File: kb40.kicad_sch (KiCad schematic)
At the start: 79 parts, among them SW1 Choc, SW10 Choc, SW11 Choc, SW12 Choc, SW13 Choc, SW14 Choc, SW15 Choc, SW16 Choc, SW17 Choc, SW18 Choc, SW19 Choc, SW2 Choc, SW20 Choc, SW21 Choc, SW22 Choc, SW23 Choc, SW24 Choc, SW3 Choc, SW4 Choc, SW5 Choc, SW6 Choc, SW7 Choc, SW8 Choc, SW9 Choc, U1 ProMicro

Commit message: initial layout
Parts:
- removed LED25, LED26, LED27, LED28, LED29, LED30: SK6812MINI-E, LED_SMD:LED_SK6812MINI_PLCC4_3.5x3.5mm_P1.75mm, symbol LED:SK6812MINI
- D1, D10, D11, D12, D13, D14, D15, D16, D17, D18, D19, D2, D20, D21, D22, D23, D24, D3, D4, D5, D6, D7, D8, D9: footprint (none) -> reversible-kicad-footprints:D_SOD-123
- LED1, LED10, LED11, LED12, LED13, LED14, LED15, LED16, LED17, LED18, LED19, LED2, LED20, LED21, LED22, LED23, LED24, LED3, LED4, LED5, LED6, LED7, LED8, LED9: footprint LED_SMD:LED_SK6812MINI_PLCC4_3.5x3.5mm_P1.75mm -> tufourn-components:SK6812Mini-E
- SW1, SW10, SW11, SW12, SW13, SW14, SW15, SW16, SW17, SW18, SW19, SW2, SW20, SW21, SW22, SW23, SW24, SW3, SW4, SW5, SW6, SW7, SW8, SW9: footprint (none) -> tufourn-components:Kailh_socket_PG1350_reversible
- U1: footprint (none) -> pro-micro:ProMicro
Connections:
- net LED: now reaches LED1.3 (DIN)
- no-connect marks 0 -> 1

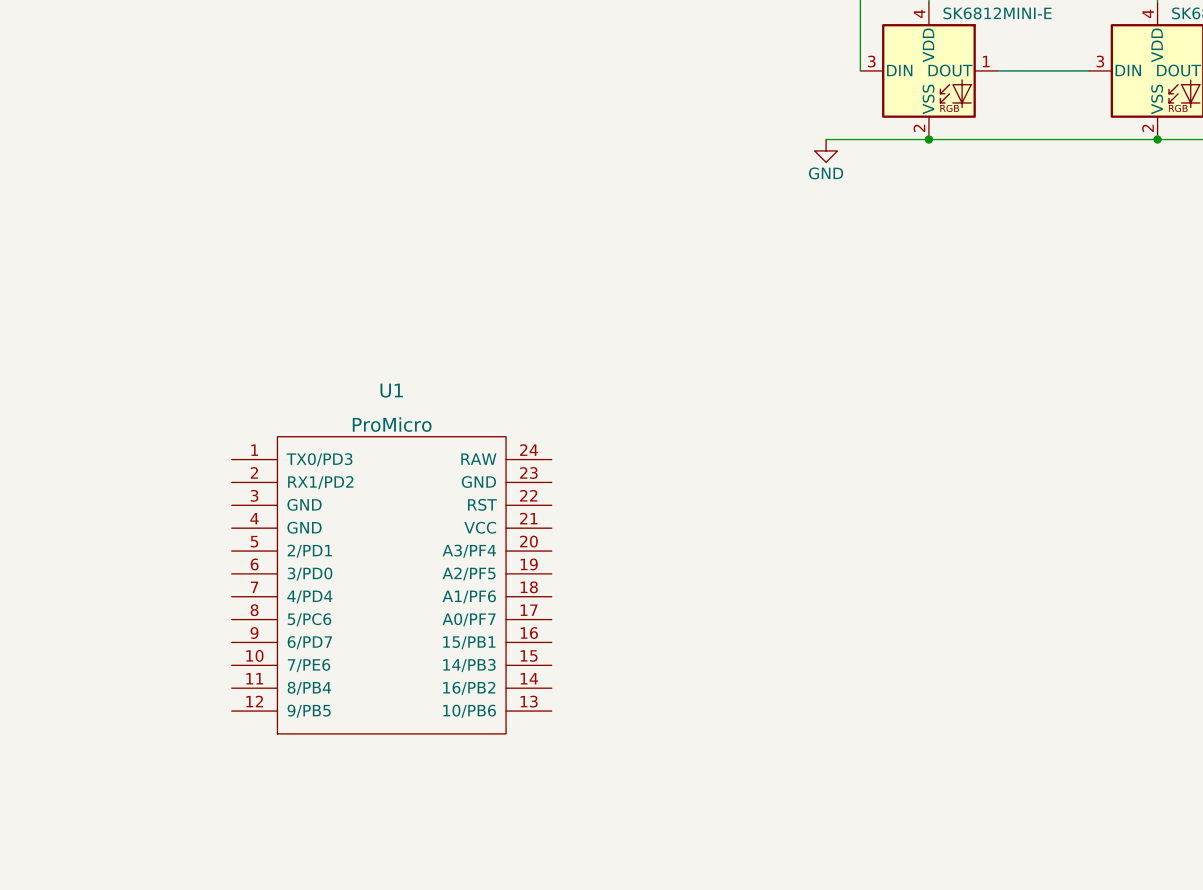
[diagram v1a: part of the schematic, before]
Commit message: initial matrix routing
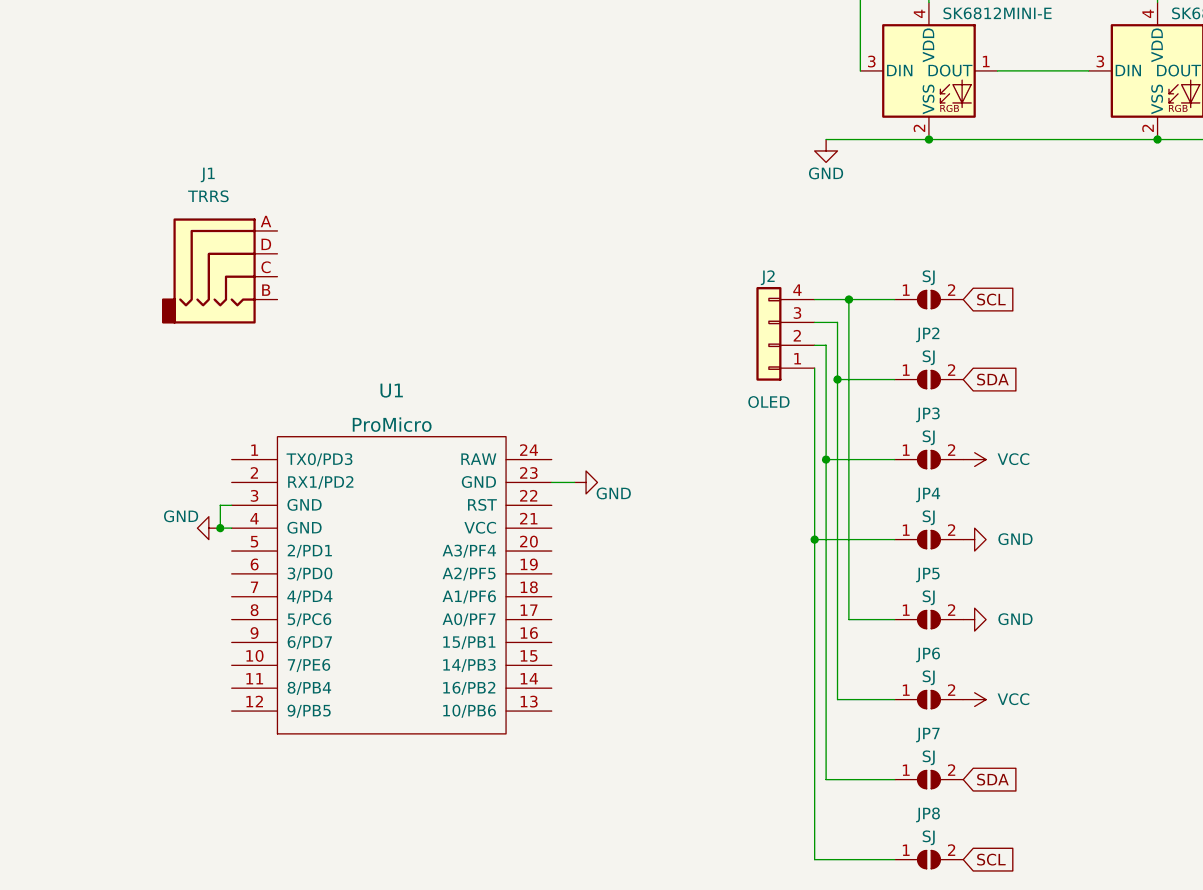
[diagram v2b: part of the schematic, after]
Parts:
- added J1: TRRS, pro-micro:PJ-320A, symbol Connector:AudioJack4
- added J2: OLED, Connector_PinSocket_2.54mm:PinSocket_1x04_P2.54mm_Vertical, symbol Connector_Generic:Conn_01x04
- added JP1, JP2, JP3, JP4, JP5, JP6, JP7, JP8: SJ, Jumper:SolderJumper-2_P1.3mm_Open_TrianglePad1.0x1.5mm, symbol Jumper:SolderJumper_2_Open
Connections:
- net GND: now also U1.23 (GND), U1.3 (GND), U1.4 (GND), JP4.2 (B), JP5.2 (B)
- new net: J2.4 (Pin_4), JP1.1 (A), JP5.1 (A)
- new net: J2.2 (Pin_2), JP3.1 (A), JP7.1 (A)
- new net: J2.3 (Pin_3), JP2.1 (A), JP6.1 (A)
- new net: J2.1 (Pin_1), JP4.1 (A), JP8.1 (A)
- new net SCL: JP1.2 (B), JP8.2 (B)
- new net SDA: JP2.2 (B), JP7.2 (B)
- new net VCC: JP3.2 (B), JP6.2 (B)

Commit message: initial rgb routing
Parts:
- LED1, LED10, LED11, LED12, LED13, LED14, LED15, LED16, LED17, LED18, LED19, LED2, LED20, LED21, LED22, LED23, LED24, LED3, LED4, LED5, LED6, LED7, LED8, LED9: footprint tufourn-components:SK6812Mini-E -> tufourn-components:SK6812-MINI-E
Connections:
- net VDD is gone; now on net VCC: LED1.4 (VDD), LED10.4 (VDD), LED11.4 (VDD), LED12.4 (VDD), LED13.4 (VDD), LED14.4 (VDD), LED15.4 (VDD), LED16.4 (VDD), LED17.4 (VDD), LED18.4 (VDD), LED19.4 (VDD), LED2.4 (VDD), LED20.4 (VDD), LED21.4 (VDD), LED22.4 (VDD), LED23.4 (VDD), LED24.4 (VDD), LED3.4 (VDD), LED4.4 (VDD), LED5.4 (VDD), LED6.4 (VDD), LED7.4 (VDD), LED8.4 (VDD), LED9.4 (VDD)
- net VCC: now also U1.21 (VCC)

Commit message: initial completed routing
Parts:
- J1: footprint pro-micro:PJ-320A -> tufourn-components:PJ-320A
- U1: footprint pro-micro:ProMicro -> tufourn-components:ArduinoProMicro-BackSide
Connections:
- net COL1: now also U1.17 (A0/PF7)
- net COL2: now also U1.9 (6/PD7)
- net COL3: now also U1.16 (15/PB1)
- net COL4: now also U1.7 (4/PD4)
- net COL5: now also U1.19 (A2/PF5)
- net GND: now also J1.D
- net LED: now also U1.1 (TX0/PD3)
- net ROW0: now also U1.20 (A3/PF4)
- net ROW1: now also U1.18 (A1/PF6)
- net ROW2: now also U1.8 (5/PC6)
- net ROW3: now also U1.15 (14/PB3)
- net SCL: now also U1.6 (3/PD0)
- net SDA: now also U1.5 (2/PD1)
- net VCC: now also J1.B
- net D2: now reaches U1.2 (RX1/PD2)
- net D2: now also J1.C
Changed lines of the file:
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@@
+    (stroke (width 0) (type default) (color 0 0 0 0))
+  )
+  (wire (pts (xy 45.72 143.51) (xy 50.8 143.51))
     (stroke (width 0) (type default) (color 0 0 0 0))
   )
@@
     (stroke (width 0) (type default) (color 0 0 0 0))
   )
+  (wire (pts (xy 45.72 156.21) (xy 50.8 156.21))
+    (stroke (width 0) (type default) (color 0 0 0 0))
+  )
   (wire (pts (xy 35.56 62.23) (xy 35.56 63.5))
     (stroke (width 0) (type default) (color 0 0 0 0))
@@
     (stroke (width 0) (type default) (color 0 0 0 0))
   )
+  (wire (pts (xy 45.72 151.13) (xy 50.8 151.13))
+    (stroke (width 0) (type default) (color 0 0 0 0))
+  )
   (wire (pts (xy 212.09 74.93) (xy 222.25 74.93))
     (stroke (width 0) (type default) (color 0 0 0 0))
   )
+  (wire (pts (xy 45.72 140.97) (xy 50.8 140.97))
+    (stroke (width 0) (type default) (color 0 0 0 0))
+  )
   (wire (pts (xy 153.67 19.05) (xy 179.07 19.05))
     (stroke (width 0) (type default) (color 0 0 0 0))
@@
   )
   (wire (pts (xy 128.27 87.63) (xy 153.67 87.63))
+    (stroke (width 0) (type default) (color 0 0 0 0))
+  )
+  (wire (pts (xy 57.15 120.65) (xy 55.88 120.65))
+    (stroke (width 0) (type default) (color 0 0 0 0))
+  )
+  (wire (pts (xy 45.72 153.67) (xy 50.8 153.67))
     (stroke (width 0) (type default) (color 0 0 0 0))
   )
@@
     )
   )
+  (global_label "ROW2" (shape input) (at 50.8 158.75 180) (fields_autoplaced)
+    (effects (font (size 1.27 1.27)) (justify right))
+    (property "Intersheet References" "${INTERSHEET_REFS}" (id 0) (at 43.1255 158.6706 0)
+      (effects (font (size 1.27 1.27)) (justify right) hide)
+    )
+  )
   (global_label "SDA" (shape input) (at 132.08 132.08 0) (fields_autoplaced)
     (effects (font (size 1.27 1.27)) (justify left))
@@
     )
   )
+  (global_label "COL2" (shape input) (at 50.8 161.29 180) (fields_autoplaced)
+    (effects (font (size 1.27 1.27)) (justify right))
+    (property "Intersheet References" "${INTERSHEET_REFS}" (id 0) (at 43.5488 161.3694 0)
+      (effects (font (size 1.27 1.27)) (justify right) hide)
+    )
+  )
+  (global_label "COL3" (shape input) (at 86.36 161.29 0) (fields_autoplaced)
+    (effects (font (size 1.27 1.27)) (justify left))
+    (property "Intersheet References" "${INTERSHEET_REFS}" (id 0) (at 93.6112 161.2106 0)
+      (effects (font (size 1.27 1.27)) (justify left) hide)
+    )
+  )
+  (global_label "COL5" (shape input) (at 86.36 153.67 0) (fields_autoplaced)
+    (effects (font (size 1.27 1.27)) (justify left))
+    (property "Intersheet References" "${INTERSHEET_REFS}" (id 0) (at 93.6112 153.5906 0)
+      (effects (font (size 1.27 1.27)) (justify left) hide)
+    )
+  )
+  (global_label "LED" (shape input) (at 45.72 140.97 180) (fields_autoplaced)
+    (effects (font (size 1.27 1.27)) (justify right))
+    (property "Intersheet References" "${INTERSHEET_REFS}" (id 0) (at 39.8598 140.8906 0)
+      (effects (font (size 1.27 1.27)) (justify right) hide)
+    )
+  )
   (global_label "LED" (shape input) (at 120.65 29.21 180) (fields_autoplaced)
     (effects (font (size 1.27 1.27)) (justify right))
@@
     )
   )
+  (global_label "COL4" (shape input) (at 45.72 156.21 180) (fields_autoplaced)
+    (effects (font (size 1.27 1.27)) (justify right))
+    (property "Intersheet References" "${INTERSHEET_REFS}" (id 0) (at 38.4688 156.2894 0)
+      (effects (font (size 1.27 1.27)) (justify right) hide)
+    )
+  )
+  (global_label "D2" (shape input) (at 45.72 143.51 180) (fields_autoplaced)
+    (effects (font (size 1.27 1.27)) (justify right))
+    (property "Intersheet References" "${INTERSHEET_REFS}" (id 0) (at 40.8274 143.4306 0)
+      (effects (font (size 1.27 1.27)) (justify right) hide)
+    )
+  )
   (global_label "SCL" (shape input) (at 132.08 185.42 0) (fields_autoplaced)
     (effects (font (size 1.27 1.27)) (justify left))
@@
     )
   )
+  (global_label "SDA" (shape input) (at 45.72 151.13 180) (fields_autoplaced)
+    (effects (font (size 1.27 1.27)) (justify right))
+    (property "Intersheet References" "${INTERSHEET_REFS}" (id 0) (at 39.7388 151.2094 0)
+      (effects (font (size 1.27 1.27)) (justify right) hide)
+    )
+  )
+  (global_label "ROW1" (shape input) (at 86.36 156.21 0) (fields_autoplaced)
+    (effects (font (size 1.27 1.27)) (justify left))
+    (property "Intersheet References" "${INTERSHEET_REFS}" (id 0) (at 94.0345 156.2894 0)
+      (effects (font (size 1.27 1.27)) (justify left) hide)
+    )
+  )
   (global_label "COL5" (shape input) (at 97.79 25.4 90) (fields_autoplaced)
     (effects (font (size 1.27 1.27)) (justify left))
@@
     )
   )
+  (global_label "ROW3" (shape input) (at 86.36 163.83 0) (fields_autoplaced)
+    (effects (font (size 1.27 1.27)) (justify left))
+    (property "Intersheet References" "${INTERSHEET_REFS}" (id 0) (at 94.0345 163.9094 0)
+      (effects (font (size 1.27 1.27)) (justify left) hide)
+    )
+  )
   (global_label "ROW2" (shape input) (at 30.48 68.58 180) (fields_autoplaced)
     (effects (font (size 1.27 1.27)) (justify right))
@@
     )
   )
+  (global_label "ROW0" (shape input) (at 86.36 151.13 0) (fields_autoplaced)
+    (effects (font (size 1.27 1.27)) (justify left))
+    (property "Intersheet References" "${INTERSHEET_REFS}" (id 0) (at 94.0345 151.2094 0)
+      (effects (font (size 1.27 1.27)) (justify left) hide)
+    )
+  )
+  (global_label "COL1" (shape input) (at 86.36 158.75 0) (fields_autoplaced)
+    (effects (font (size 1.27 1.27)) (justify left))
+    (property "Intersheet References" "${INTERSHEET_REFS}" (id 0) (at 93.6112 158.6706 0)
+      (effects (font (size 1.27 1.27)) (justify left) hide)
+    )
+  )
+  (global_label "D2" (shape input) (at 57.15 120.65 0) (fields_autoplaced)
+    (effects (font (size 1.27 1.27)) (justify left))
+    (property "Intersheet References" "${INTERSHEET_REFS}" (id 0) (at 62.0426 120.7294 0)
+      (effects (font (size 1.27 1.27)) (justify left) hide)
+    )
+  )
+  (global_label "SCL" (shape input) (at 45.72 153.67 180) (fields_autoplaced)
+    (effects (font (size 1.27 1.27)) (justify right))
+    (property "Intersheet References" "${INTERSHEET_REFS}" (id 0) (at 39.7993 153.7494 0)
+      (effects (font (size 1.27 1.27)) (justify right) hide)
+    )
+  )
   (global_label "COL4" (shape input) (at 86.36 25.4 90) (fields_autoplaced)
     (effects (font (size 1.27 1.27)) (justify left))
@@
     (pin "2")
   )
+  (symbol (lib_id "power:GND") (at 55.88 118.11 90) (unit 1)
+    (in_bom yes) (on_board yes)
+    (property "Reference" "#PWR0105" (id 0) (at 62.23 118.11 0)
+      (effects (font (size 1.27 1.27)) hide)
+    )
+    (property "Value" "GND" (id 1) (at 62.23 116.84 90)
+      (effects (font (size 1.27 1.27)) (justify left))
+    )
+    (property "Footprint" "" (id 2) (at 55.88 118.11 0)
+      (effects (font (size 1.27 1.27)) hide)
+    )
+    (property "Datasheet" "" (id 3) (at 55.88 118.11 0)
+      (effects (font (size 1.27 1.27)) hide)
+    )
+    (pin "1")
+  )
   (symbol (lib_id "LED:SK6812MINI") (at 153.67 74.93 0) (unit 1)
     (in_bom yes) (on_board yes)
@@
     (pin "1")
   )
+  (symbol (lib_id "power:VCC") (at 55.88 123.19 270) (unit 1)
+    (in_bom yes) (on_board yes) (fields_autoplaced)
+    (property "Reference" "#PWR0104" (id 0) (at 52.07 123.19 0)
+      (effects (font (size 1.27 1.27)) hide)
+    )
+    (property "Value" "VCC" (id 1) (at 59.69 123.1899 90)
+      (effects (font (size 1.27 1.27)) (justify left))
+    )
+    (property "Footprint" "" (id 2) (at 55.88 123.19 0)
+      (effects (font (size 1.27 1.27)) hide)
+    )
+    (property "Datasheet" "" (id 3) (at 55.88 123.19 0)
+      (effects (font (size 1.27 1.27)) hide)
+    )
+    (pin "1")
+  )
   (symbol (lib_id "Switch:SW_Push_45deg") (at 38.1 34.29 0) (unit 1)
     (in_bom yes) (on_board yes) (fields_autoplaced)
@@
       (effects (font (size 1.524 1.524)))
     )
-    (property "Footprint" "pro-micro:ProMicro" (id 2) (at 95.25 218.44 90)
+    (property "Footprint" "tufourn-components:ArduinoProMicro-BackSide" (id 2) (at 95.25 218.44 90)
       (effects (font (size 1.524 1.524)) hide)
     )
@@
     (property "Reference" "J1" (id 0) (at 48.26 109.22 0))
     (property "Value" "TRRS" (id 1) (at 48.26 111.76 0))
-    (property "Footprint" "pro-micro:PJ-320A" (id 2) (at 50.8 118.11 0)
+    (property "Footprint" "tufourn-components:PJ-320A" (id 2) (at 50.8 118.11 0)
       (effects (font (size 1.27 1.27)) hide)
     )
@@
       (reference "#PWR0103") (unit 1) (value "VCC") (footprint "")
     )
+    (path "/9b6bed1e-5437-4868-a38c-d0ba8e54fcaf"
+      (reference "#PWR0104") (unit 1) (value "VCC") (footprint "")
+    )
+    (path "/57fc5f0c-df2a-4a34-adcb-f91a8c44594d"
+      (reference "#PWR0105") (unit 1) (value "GND") (footprint "")
+    )
     (path "/027c28db-a8ac-4b45-8620-509e292a40dd"
       (reference "D1") (unit 1) (value "1n4148") (footprint "reversible-kicad-footprints:D_SOD-123")
@@
     )
     (path "/eed89c8c-f1ff-43c2-9aac-20ad78492145"
-      (reference "J1") (unit 1) (value "TRRS") (footprint "pro-micro:PJ-320A")
+      (reference "J1") (unit 1) (value "TRRS") (footprint "tufourn-components:PJ-320A")
     )
     (path "/69bb6d28-3ee2-4be6-b4ee-68ba04efa8b5"
@@
     )
     (path "/ed0810fc-10f9-47cf-b838-ddec329a8bc0"
-      (reference "U1") (unit 1) (value "ProMicro") (footprint "pro-micro:ProMicro")
-    )
-  )
+      (reference "U1") (unit 1) (value "ProMicro") (footprint "tufourn-components:ArduinoProMicro-BackSide")
+    )
+  )

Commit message: added silkscreen
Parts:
- D1, D10, D11, D12, D13, D14, D15, D16, D17, D18, D19, D2, D20, D21, D22, D23, D24, D3, D4, D5, D6, D7, D8, D9: footprint reversible-kicad-footprints:D_SOD-123 -> tufourn-components:D_SOD-123
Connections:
- net COL0: now also U1.10 (7/PE6)
- no-connect marks 1 -> 8

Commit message: fix i2c and generate gerbers
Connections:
- net SCL: now also JP2.2 (B), JP7.2 (B); no longer JP1.2 (B), JP8.2 (B)
- net SDA: now also JP1.2 (B), JP8.2 (B); no longer JP2.2 (B), JP7.2 (B)
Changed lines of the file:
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@@
     )
   )
-  (global_label "SDA" (shape input) (at 132.08 132.08 0) (fields_autoplaced)
+  (global_label "SDA" (shape input) (at 132.08 123.19 0) (fields_autoplaced)
     (effects (font (size 1.27 1.27)) (justify left))
-    (property "Intersheet References" "${INTERSHEET_REFS}" (id 0) (at 138.0612 132.0006 0)
+    (property "Intersheet References" "${INTERSHEET_REFS}" (id 0) (at 138.0612 123.1106 0)
       (effects (font (size 1.27 1.27)) (justify left) hide)
     )
@@
     )
   )
-  (global_label "SCL" (shape input) (at 132.08 123.19 0) (fields_autoplaced)
+  (global_label "SCL" (shape input) (at 132.08 132.08 0) (fields_autoplaced)
     (effects (font (size 1.27 1.27)) (justify left))
-    (property "Intersheet References" "${INTERSHEET_REFS}" (id 0) (at 138.0007 123.1106 0)
+    (property "Intersheet References" "${INTERSHEET_REFS}" (id 0) (at 138.0007 132.0006 0)
       (effects (font (size 1.27 1.27)) (justify left) hide)
     )
@@
     )
   )
-  (global_label "SDA" (shape input) (at 132.08 176.53 0) (fields_autoplaced)
+  (global_label "SDA" (shape input) (at 132.08 185.42 0) (fields_autoplaced)
     (effects (font (size 1.27 1.27)) (justify left))
-    (property "Intersheet References" "${INTERSHEET_REFS}" (id 0) (at 138.0612 176.4506 0)
+    (property "Intersheet References" "${INTERSHEET_REFS}" (id 0) (at 138.0612 185.3406 0)
       (effects (font (size 1.27 1.27)) (justify left) hide)
     )
@@
     )
   )
-  (global_label "SCL" (shape input) (at 132.08 185.42 0) (fields_autoplaced)
+  (global_label "SCL" (shape input) (at 132.08 176.53 0) (fields_autoplaced)
     (effects (font (size 1.27 1.27)) (justify left))
-    (property "Intersheet References" "${INTERSHEET_REFS}" (id 0) (at 138.0007 185.3406 0)
+    (property "Intersheet References" "${INTERSHEET_REFS}" (id 0) (at 138.0007 176.4506 0)
       (effects (font (size 1.27 1.27)) (justify left) hide)
     )
